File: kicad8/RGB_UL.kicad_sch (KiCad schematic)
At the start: 39 parts

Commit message: Added: Stepped CAPS_LOCK and Split backspace
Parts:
- R5: footprint (none) -> Diode_SMD:D_SOD-123
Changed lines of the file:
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@@
 			)
 		)
-		(property "Footprint" ""
+		(property "Footprint" "Diode_SMD:D_SOD-123"
 			(at 30.48 30.48 0)
 			(effects
@@
 		(dnp no)
 		(fields_autoplaced yes)
-		(property "Reference" "#PWR019"
+		(property "Reference" "#PWR017"
 			(at 34.29 26.67 0)
 			(effects
@@
 			(project "kicad8"
 				(path "/4d291fcf-fdf2-46ba-aa57-60bc75f9cc32/5ce6faf6-3b88-47dd-8c67-c3e84c0ecbb7"
-					(reference "#PWR019")
-					(unit 1)
-				)
+					(reference "#PWR017")
+					(unit 1)
+				)

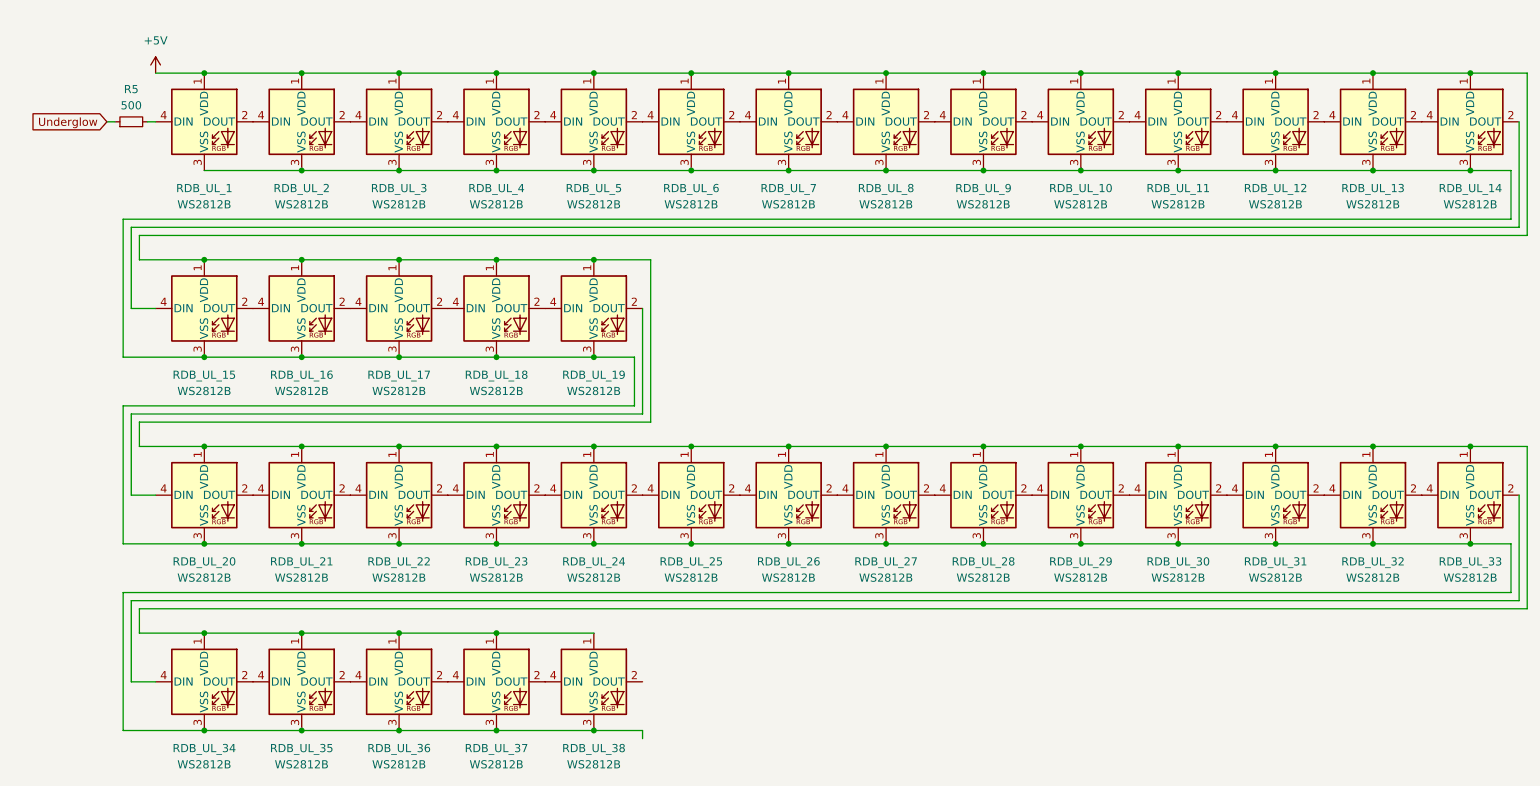
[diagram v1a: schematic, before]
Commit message: Finished: Wiring for the Switch matrix, Underglow RGB and Per-key RGb
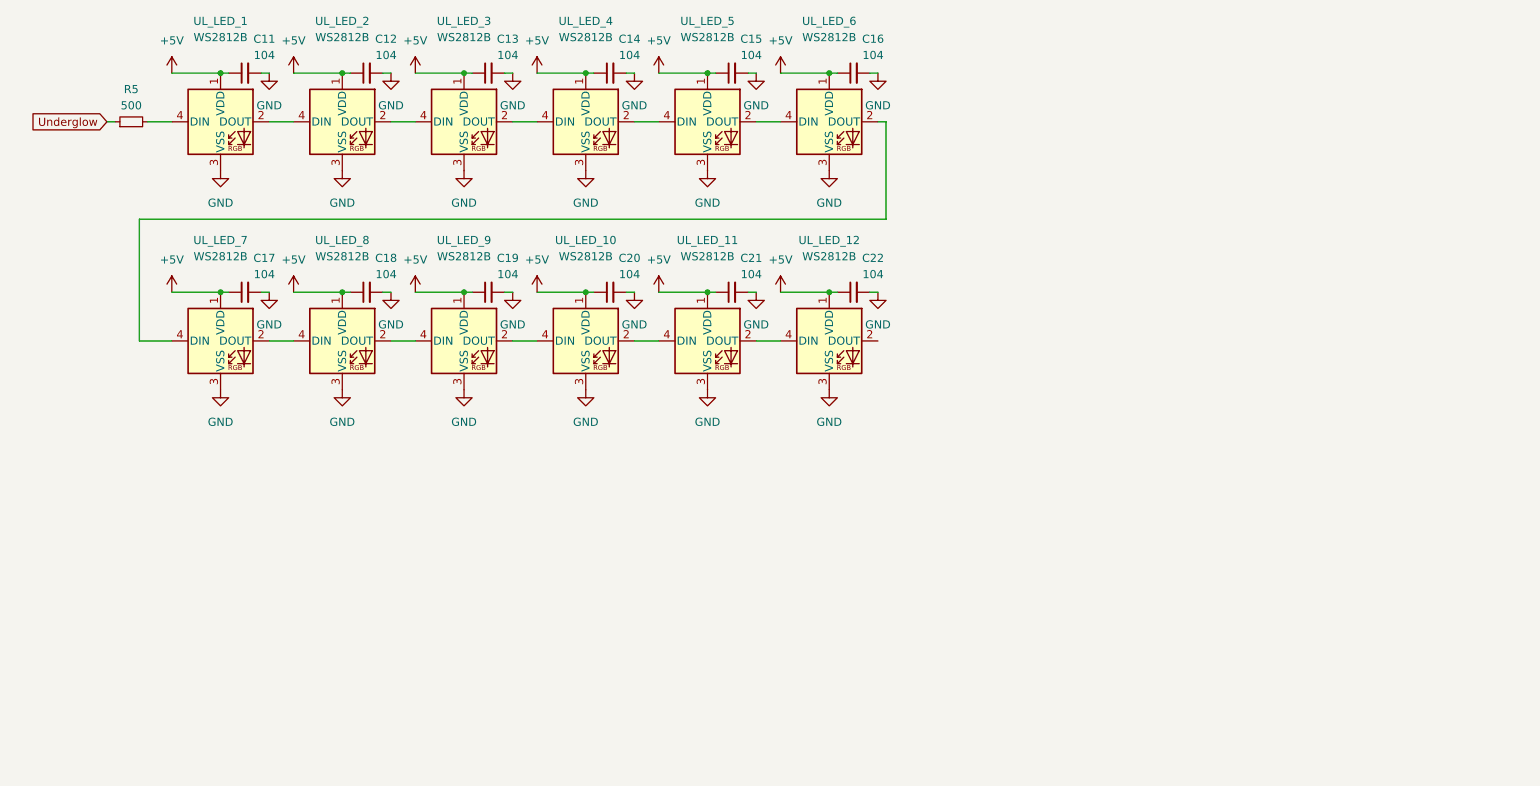
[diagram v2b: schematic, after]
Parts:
- removed RDB_UL_1, RDB_UL_10, RDB_UL_11, RDB_UL_12, RDB_UL_13, RDB_UL_14, RDB_UL_15, RDB_UL_16, RDB_UL_17, RDB_UL_18, RDB_UL_19, RDB_UL_2, RDB_UL_20, RDB_UL_21, RDB_UL_22, RDB_UL_23, RDB_UL_24, RDB_UL_25, RDB_UL_26, RDB_UL_27, RDB_UL_28, RDB_UL_29, RDB_UL_3, RDB_UL_30, RDB_UL_31, RDB_UL_32, RDB_UL_33, RDB_UL_34, RDB_UL_35, RDB_UL_36, RDB_UL_37, RDB_UL_38, RDB_UL_4, RDB_UL_5, RDB_UL_6, RDB_UL_7, RDB_UL_8, RDB_UL_9: WS2812B, LED_SMD:LED_WS2812B_PLCC4_5.0x5.0mm_P3.2mm, symbol LED:WS2812B
- added C11, C12, C13, C14, C15, C16, C17, C18, C19, C20, C21, C22: 104, Diode_SMD:D_SOD-123, symbol Device:C_Small
- added UL_LED_1, UL_LED_10, UL_LED_11, UL_LED_12, UL_LED_2, UL_LED_3, UL_LED_4, UL_LED_5, UL_LED_6, UL_LED_7, UL_LED_8, UL_LED_9: WS2812B, LED_SMD:LED_WS2812B_PLCC4_5.0x5.0mm_P3.2mm, symbol LED:WS2812B
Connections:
- net +5V: now also C11.1, C12.1, C13.1, C14.1, C15.1, C16.1, C17.1, C18.1, C19.1, C20.1, C21.1, C22.1, UL_LED_1.1 (VDD), UL_LED_10.1 (VDD), UL_LED_11.1 (VDD), UL_LED_12.1 (VDD), UL_LED_2.1 (VDD), UL_LED_3.1 (VDD), UL_LED_4.1 (VDD), UL_LED_5.1 (VDD), UL_LED_6.1 (VDD), UL_LED_7.1 (VDD), UL_LED_8.1 (VDD), UL_LED_9.1 (VDD)
- net at R5.2: now also UL_LED_1.4 (DIN)
- new net: UL_LED_6.2 (DOUT), UL_LED_7.4 (DIN)
- new net: UL_LED_5.2 (DOUT), UL_LED_6.4 (DIN)
- new net: UL_LED_4.2 (DOUT), UL_LED_5.4 (DIN)
- new net: UL_LED_10.2 (DOUT), UL_LED_11.4 (DIN)
- new net: UL_LED_10.4 (DIN), UL_LED_9.2 (DOUT)
- new net: UL_LED_7.2 (DOUT), UL_LED_8.4 (DIN)
- new net: UL_LED_3.2 (DOUT), UL_LED_4.4 (DIN)
- new net: UL_LED_2.2 (DOUT), UL_LED_3.4 (DIN)
- new net: UL_LED_11.2 (DOUT), UL_LED_12.4 (DIN)
- new net: UL_LED_8.2 (DOUT), UL_LED_9.4 (DIN)
- new net: UL_LED_1.2 (DOUT), UL_LED_2.4 (DIN)
- new net GND: C11.2, C12.2, C13.2, C14.2, C15.2, C16.2, C17.2, C18.2, C19.2, C20.2, C21.2, C22.2, UL_LED_1.3 (VSS), UL_LED_10.3 (VSS), UL_LED_11.3 (VSS), UL_LED_12.3 (VSS), UL_LED_2.3 (VSS), UL_LED_3.3 (VSS), UL_LED_4.3 (VSS), UL_LED_5.3 (VSS), UL_LED_6.3 (VSS), UL_LED_7.3 (VSS), UL_LED_8.3 (VSS), UL_LED_9.3 (VSS)

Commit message: Added: MOSFET for encoder and drill holes for case
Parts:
- renumbered R5 to R6
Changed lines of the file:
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@@
 		(dnp no)
 		(fields_autoplaced yes)
-		(property "Reference" "R5"
+		(property "Reference" "R6"
 			(at 30.48 25.4 90)
 			(effects
@@
 			(project ""
 				(path "/4d291fcf-fdf2-46ba-aa57-60bc75f9cc32/5ce6faf6-3b88-47dd-8c67-c3e84c0ecbb7"
-					(reference "R5")
+					(reference "R6")
 					(unit 1)
 				)
@@
 		(dnp no)
 		(fields_autoplaced yes)
-		(property "Reference" "#PWR017"
+		(property "Reference" "#PWR018"
 			(at 36.83 26.67 0)
 			(effects
@@
 			(project ""
 				(path "/4d291fcf-fdf2-46ba-aa57-60bc75f9cc32/5ce6faf6-3b88-47dd-8c67-c3e84c0ecbb7"
-					(reference "#PWR017")
-					(unit 1)
-				)
+					(reference "#PWR018")
+					(unit 1)
+				)

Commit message: Removed: old RGB file
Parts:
- C11, C12, C13, C14, C15, C16, C17, C18, C19, C20, C21, C22: footprint Diode_SMD:D_SOD-123 -> Capacitor_SMD:C_0402_1005Metric
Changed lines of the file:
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@@
 			)
 		)
-		(property "Footprint" "Diode_SMD:D_SOD-123"
+		(property "Footprint" "Capacitor_SMD:C_0402_1005Metric"
 			(at 67.31 22.86 0)
 			(effects
@@
 			)
 		)
-		(property "Footprint" "Diode_SMD:D_SOD-123"
+		(property "Footprint" "Capacitor_SMD:C_0402_1005Metric"
 			(at 67.31 57.15 0)
 			(effects
@@
 			)
 		)
-		(property "Footprint" "Diode_SMD:D_SOD-123"
+		(property "Footprint" "Capacitor_SMD:C_0402_1005Metric"
 			(at 86.36 22.86 0)
 			(effects
@@
 			)
 		)
-		(property "Footprint" "Diode_SMD:D_SOD-123"
+		(property "Footprint" "Capacitor_SMD:C_0402_1005Metric"
 			(at 124.46 57.15 0)
 			(effects
@@
 			)
 		)
-		(property "Footprint" "Diode_SMD:D_SOD-123"
+		(property "Footprint" "Capacitor_SMD:C_0402_1005Metric"
 			(at 48.26 57.15 0)
 			(effects
@@
 			)
 		)
-		(property "Footprint" "Diode_SMD:D_SOD-123"
+		(property "Footprint" "Capacitor_SMD:C_0402_1005Metric"
 			(at 48.26 22.86 0)
 			(effects
@@
 			)
 		)
-		(property "Footprint" "Diode_SMD:D_SOD-123"
+		(property "Footprint" "Capacitor_SMD:C_0402_1005Metric"
 			(at 105.41 22.86 0)
 			(effects
@@
 			)
 		)
-		(property "Footprint" "Diode_SMD:D_SOD-123"
+		(property "Footprint" "Capacitor_SMD:C_0402_1005Metric"
 			(at 143.51 57.15 0)
 			(effects
@@
 			)
 		)
-		(property "Footprint" "Diode_SMD:D_SOD-123"
+		(property "Footprint" "Capacitor_SMD:C_0402_1005Metric"
 			(at 86.36 57.15 0)
 			(effects
@@
 			)
 		)
-		(property "Footprint" "Diode_SMD:D_SOD-123"
+		(property "Footprint" "Capacitor_SMD:C_0402_1005Metric"
 			(at 105.41 57.15 0)
 			(effects
@@
 			)
 		)
-		(property "Footprint" "Diode_SMD:D_SOD-123"
+		(property "Footprint" "Capacitor_SMD:C_0402_1005Metric"
 			(at 143.51 22.86 0)
 			(effects
@@
 			)
 		)
-		(property "Footprint" "Diode_SMD:D_SOD-123"
+		(property "Footprint" "Capacitor_SMD:C_0402_1005Metric"
 			(at 124.46 22.86 0)
 			(effects

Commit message: Initial branch commit
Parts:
- R6: footprint Diode_SMD:D_SOD-123 -> Resistor_SMD:R_0402_1005Metric
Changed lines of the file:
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@@
 			)
 		)
-		(property "Footprint" "Diode_SMD:D_SOD-123"
+		(property "Footprint" "Resistor_SMD:R_0402_1005Metric"
 			(at 30.48 30.48 0)
 			(effects
